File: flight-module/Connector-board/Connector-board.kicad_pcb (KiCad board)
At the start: 4 copper layers, 0 parts

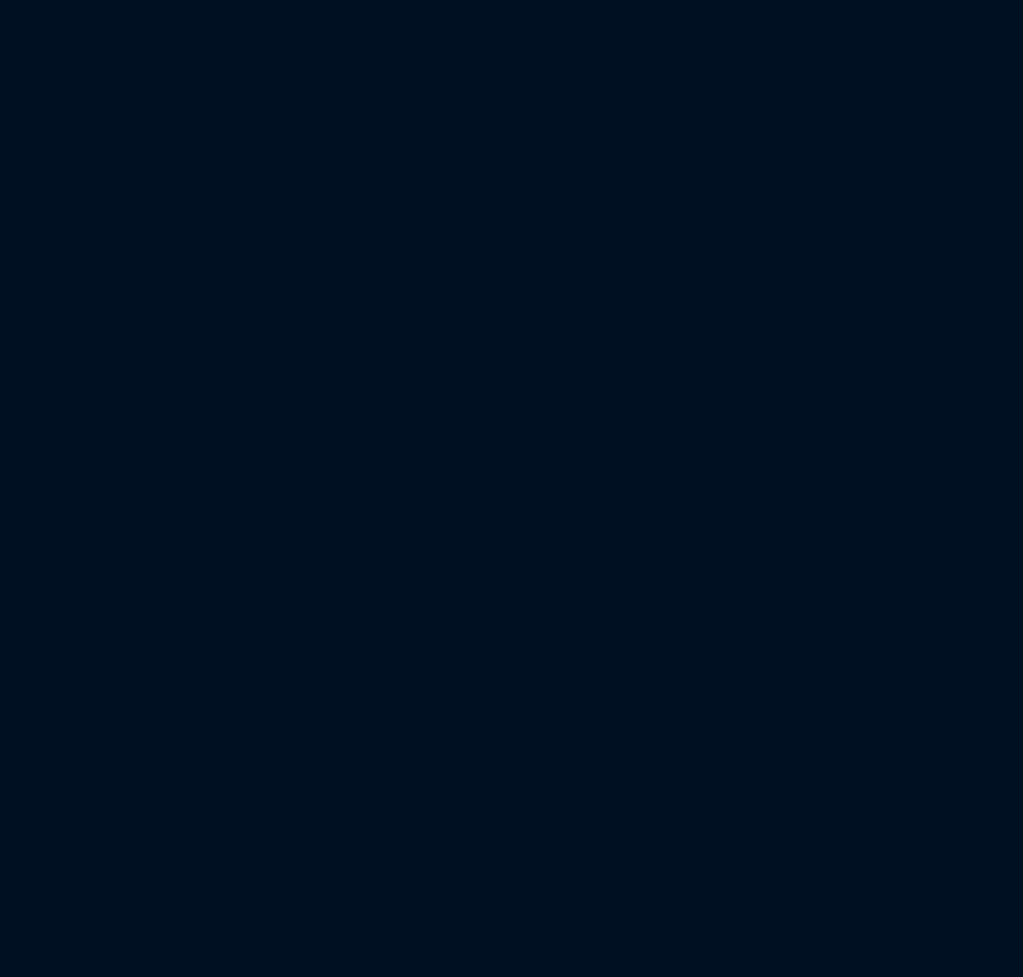
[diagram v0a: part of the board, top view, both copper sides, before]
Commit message: Edited the connector board to make sense
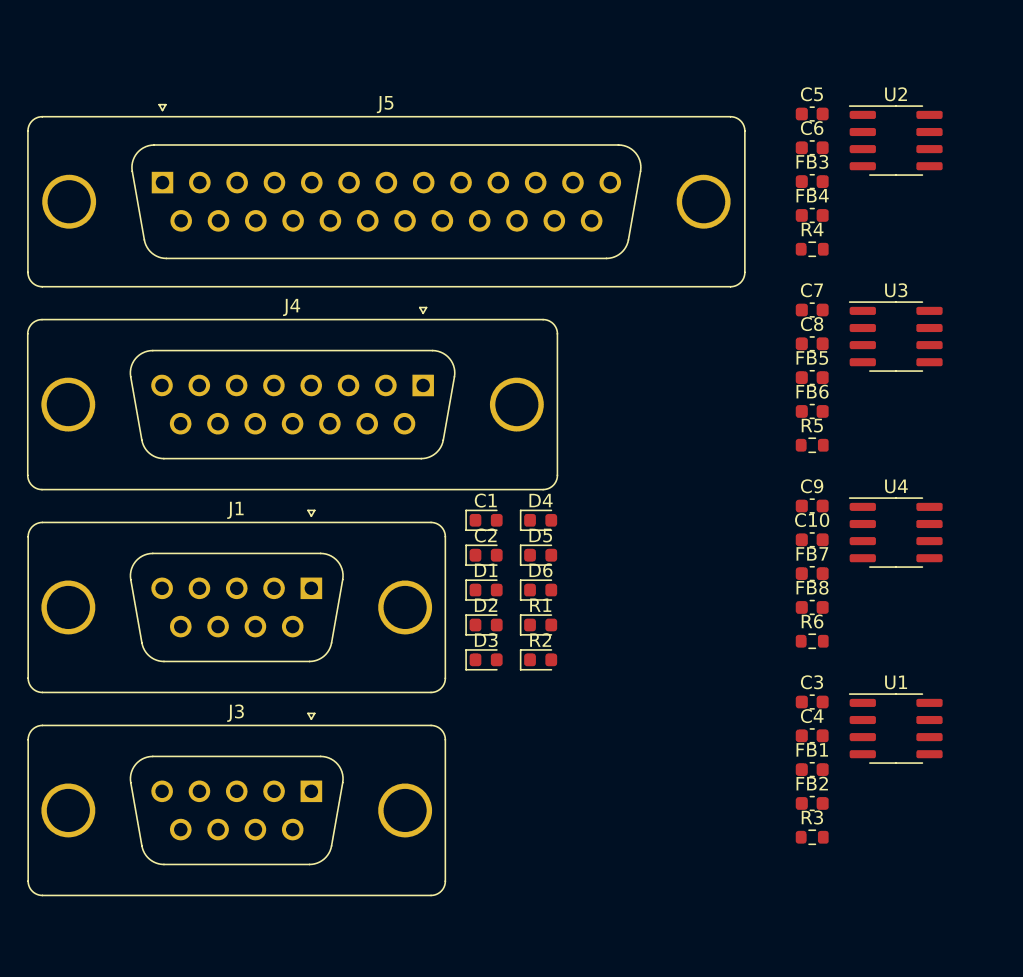
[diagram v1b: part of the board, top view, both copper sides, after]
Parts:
- added C1: 22 µF, Diode_SMD:D_0603_1608Metric, F.Cu at (165.2, 99.5)
- added C10: 10u, Capacitor_SMD:C_0603_1608Metric, F.Cu at (189.4, 100.9)
- added C2: 22 µF, Diode_SMD:D_0603_1608Metric, F.Cu at (165.2, 102.1)
- added C3: 0.01u, Capacitor_SMD:C_0603_1608Metric, F.Cu at (189.4, 113.0)
- added C4: 10u, Capacitor_SMD:C_0603_1608Metric, F.Cu at (189.4, 115.5)
- added C5: 0.01u, Capacitor_SMD:C_0603_1608Metric, F.Cu at (189.4, 69.3)
- added C6: 10u, Capacitor_SMD:C_0603_1608Metric, F.Cu at (189.4, 71.8)
- added C7: 0.01u, Capacitor_SMD:C_0603_1608Metric, F.Cu at (189.4, 83.9)
- added C8: 10u, Capacitor_SMD:C_0603_1608Metric, F.Cu at (189.4, 86.4)
- added C9: 0.01u, Capacitor_SMD:C_0603_1608Metric, F.Cu at (189.4, 98.4)
- added D1: D_Schottky, Diode_SMD:D_0603_1608Metric, F.Cu at (165.2, 104.7)
- added D2: D_Schottky, Diode_SMD:D_0603_1608Metric, F.Cu at (165.2, 107.2)
- added D3: D_Schottky, Diode_SMD:D_0603_1608Metric, F.Cu at (165.2, 109.8)
- added D4: D_Schottky, Diode_SMD:D_0603_1608Metric, F.Cu at (169.3, 99.5)
- added D5: D_Schottky, Diode_SMD:D_0603_1608Metric, F.Cu at (169.3, 102.1)
- added D6: D_Schottky, Diode_SMD:D_0603_1608Metric, F.Cu at (169.3, 104.7)
- added FB1: FerriteBead_Small, Capacitor_SMD:C_0603_1608Metric, F.Cu at (189.4, 118.0)
- added FB2: FerriteBead_Small, Capacitor_SMD:C_0603_1608Metric, F.Cu at (189.4, 120.5)
- added FB3: FerriteBead_Small, Capacitor_SMD:C_0603_1608Metric, F.Cu at (189.4, 74.3)
- added FB4: FerriteBead_Small, Capacitor_SMD:C_0603_1608Metric, F.Cu at (189.4, 76.8)
- added FB5: FerriteBead_Small, Capacitor_SMD:C_0603_1608Metric, F.Cu at (189.4, 88.9)
- added FB6: FerriteBead_Small, Capacitor_SMD:C_0603_1608Metric, F.Cu at (189.4, 91.4)
- added FB7: FerriteBead_Small, Capacitor_SMD:C_0603_1608Metric, F.Cu at (189.4, 103.4)
- added FB8: FerriteBead_Small, Capacitor_SMD:C_0603_1608Metric, F.Cu at (189.4, 105.9)
- added J1: DB9_Female, Connector_Dsub:DSUB-9_Female_Vertical_P2.77x2.84mm_MountingHoles, F.Cu at (152.2, 104.5)
- added J3: DB9_Female, Connector_Dsub:DSUB-9_Female_Vertical_P2.77x2.84mm_MountingHoles, F.Cu at (152.2, 119.6)
- added J4: DB15_Female, Connector_Dsub:DSUB-15_Female_Vertical_P2.77x2.84mm_MountingHoles, F.Cu at (160.5, 89.5)
- added J5: DB25_Receptacle, Connector_Dsub:DSUB-25_Male_Vertical_P2.77x2.84mm_MountingHoles, F.Cu at (141.2, 74.4)
- added R1: 1k, Diode_SMD:D_0603_1608Metric, F.Cu at (169.3, 107.2)
- added R2: 1k, Diode_SMD:D_0603_1608Metric, F.Cu at (169.3, 109.8)
- added R3: 10k, Resistor_SMD:R_0603_1608Metric, F.Cu at (189.4, 123.0)
- added R4: 10k, Resistor_SMD:R_0603_1608Metric, F.Cu at (189.4, 79.4)
- added R5: 10k, Resistor_SMD:R_0603_1608Metric, F.Cu at (189.4, 93.9)
- added R6: 10k, Resistor_SMD:R_0603_1608Metric, F.Cu at (189.4, 108.5)
- added U1: MAX31855KASA, Package_SO:SOIC-8_3.9x4.9mm_P1.27mm, F.Cu at (195.6, 114.9)
- added U2: MAX31855KASA, Package_SO:SOIC-8_3.9x4.9mm_P1.27mm, F.Cu at (195.6, 71.3)
- added U3: MAX31855KASA, Package_SO:SOIC-8_3.9x4.9mm_P1.27mm, F.Cu at (195.6, 85.8)
- added U4: MAX31855KASA, Package_SO:SOIC-8_3.9x4.9mm_P1.27mm, F.Cu at (195.6, 100.4)
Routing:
- net (no net): track 0.00 -> 5309.5 mm
- net 12V: track 363.1 -> 0.00 mm
- net HX5: track 297.7 -> 0.00 mm
- net 3.3V: track 293.4 -> 0.00 mm
- net HX CLK: track 262.4 -> 0.00 mm
- net HX3: track 262.4 -> 0.00 mm
- net SD, TC MISO: track 262.3 -> 0.00 mm
- net HX7: track 241.6 -> 0.00 mm
- net HX1: track 237.9 -> 0.00 mm
- net HX6: track 236.2 -> 0.00 mm
- net HX8: track 233.8 -> 0.00 mm
- net SD, TC CLK: track 228.3 -> 0.00 mm
- net TC CLK: track 223.3 -> 0.00 mm
- net TC MISO: track 215.4 -> 0.00 mm
- net 5V: track 211.1 -> 0.00 mm
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
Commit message: commit edits to the schematic to reflect new pinouts
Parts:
- added J2: Stack_Shape, Stack_Shape:Stack_Shape, F.Cu at (167.6, 94.0)
- moved J5 44.2 mm to (182.4, 58.4), turned to 180 degrees
- moved J3 28.6 mm to (145.9, 91.7), turned to 180 degrees
- moved U2 20.3 mm to (198.1, 91.4)
- moved C4 19.2 mm to (189.4, 134.7)
- moved R3 19.2 mm to (189.4, 142.2)
- moved FB1 19.2 mm to (189.4, 137.2)
- moved FB2 19.2 mm to (189.4, 139.7)
- moved U3 19.1 mm to (198.1, 104.8)
- moved U4 18.5 mm to (198.1, 118.7)
- moved C1 17.5 mm to (165.2, 117.0)
- moved C7 17.5 mm to (189.4, 101.3)
- moved C8 17.5 mm to (189.4, 103.9)
- moved D4 17.5 mm to (169.2, 117.0)
- moved FB6 17.5 mm to (189.4, 108.9)
- moved R5 17.5 mm to (189.4, 111.4)
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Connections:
- net /ETH_Vent renamed /ETH_VENT
- net /LOX_Vent renamed /LOX_VENT
- D1 pad 2: /Ground_ETH_Vent -> GROUND_ETH_VENT
- D2 pad 2: /REDS_ETH_Vent -> REDS_ETH_VENT
- D3 pad 2: /Flight_ETH_Vent -> FLIGHT_ETH_VENT
- D4 pad 2: /Ground_LOX_Vent -> GROUND_LOX_VENT
- D5 pad 2: /REDS_LOX_Vent -> REDS_LOX_VENT
- D6 pad 2: /Flight_LOX_Vent -> FLIGHT_LOX_VENT
- J4 pad 12: REDS_GND -> GND
- J4 pad 13: REDS_ETH -> REDS_ETH_VENT
- J4 pad 14: REDS_LOX_VENT -> GROUND_LOX_VENT
- J4 pad 6: GROUND_LOX_VENT -> REDS_LOX_VENT
- R1 pad 2: GND2 -> GND
- R2 pad 2: GND2 -> GND
- U1 pad 5: SPI1_SCK -> SPI_SCK
- U1 pad 7: SPI1_MISO -> SPI_MISO
- U2 pad 5: SP4_SCK -> SPI_SCK
- U2 pad 7: SP4_MISO -> SPI_MISO
- U3 pad 5: SP2_SCK -> SPI_SCK
- U3 pad 7: SP2_MISO -> SPI_MISO
- U4 pad 5: SPI3_SCK -> SPI_SCK
- U4 pad 7: SPI3_MISO -> SPI_MISO
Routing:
- net (no net): track 5309.5 -> 0.00 mm
- net GND: track 350.6 -> 0.00 mm
- net unconnected-(J5-P25-Pad25): track 47.6 -> 0.00 mm
- net +3.3V: track 28.6 -> 0.00 mm
- net unconnected-(J5-Pad13): track 7.00 -> 0.00 mm
- net TC1_CS: track 0.00 -> 3.46 mm
- net PT1_E+: track 0.00 -> 2.53 mm
- net PT3_A+: track 0.00 -> 0.56 mm
- added copper zone on In2.Cu, net +3.3V
- added copper zone on In1.Cu, net GND
- removed copper zone on B.Cu, net GND
- removed copper zone on F.Cu, net GND
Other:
- board outline added: 141.7 x 134.1 mm

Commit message: completed routing
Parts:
- removed J2: Stack_Shape, Stack_Shape:Stack_Shape
- added J1: Stack_Shape, Stack_Shape:Stack_Shape, F.Cu at (172.7, 106.8)
- D1, D2, D3, D4, D5, D6: footprint Diode_SMD:D_0603_1608Metric -> Diode_SMD:D_SOD-128
- moved U1 84.4 mm to (117.9, 106.1), turned to 90 degrees
- moved C4 80.1 mm to (118.1, 98.2), turned to 180 degrees
- moved FB2 76.1 mm to (117.7, 114.3), turned to 90 degrees
- moved R3 75.7 mm to (122.9, 106.1), turned to -90 degrees
- moved C3 73.4 mm to (118.6, 111.2), turned to 180 degrees
- moved FB1 73.1 mm to (120.0, 114.3), turned to 90 degrees
- moved U4 71.2 mm to (128.0, 106.1), turned to 90 degrees
- moved C10 64.6 mm to (128.1, 98.0), turned to 180 degrees
- moved GND_DSUB1 63.4 mm to (204.2, 124.3), turned to 0 degrees
- moved FB8 62.5 mm to (127.5, 114.5), turned to 90 degrees
- moved C9 61.6 mm to (128.0, 111.2), turned to 180 degrees
- moved FB7 60.0 mm to (129.7, 114.6), turned to 90 degrees
- moved U3 60.0 mm to (138.2, 106.1), turned to 90 degrees
- moved R6 59.7 mm to (133.1, 106.1), turned to -90 degrees
- moved FB6 53.2 mm to (136.5, 114.6), turned to 90 degrees
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- renumbered J3 to 4TC_DSUB1, J4 to GND_DSUB1, J5 to PT_DSUB1, J1 to SOLENOIDS_DSUB1
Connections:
- C1 pad 1: /ETH_VENT -> ETH_VENT
- C2 pad 1: /LOX_VENT -> LOX_VENT
- D1 pad 1: /ETH_VENT -> ETH_VENT
- D2 pad 1: /ETH_VENT -> ETH_VENT
- D3 pad 1: /ETH_VENT -> ETH_VENT
- D4 pad 1: /LOX_VENT -> LOX_VENT
- D5 pad 1: /LOX_VENT -> LOX_VENT
- D6 pad 1: /LOX_VENT -> LOX_VENT
- GND_DSUB1 pad 14: GROUND_LOX_VENT -> REDS_LOX_VENT
- GND_DSUB1 pad 6: REDS_LOX_VENT -> GROUND_LOX_VENT
- PT_DSUB1 pad 10: unconnected-(J5-Pad10) -> PT5_E-
- PT_DSUB1 pad 11: unconnected-(J5-Pad11) -> PT6_E+
- PT_DSUB1 pad 12: unconnected-(J5-Pad12) -> PT6_E-
- PT_DSUB1 pad 15: PT2_E- -> unconnected-(PT_DSUB1-P15-Pad15)
- PT_DSUB1 pad 17: PT3_A+ -> unconnected-(PT_DSUB1-P17-Pad17)
- PT_DSUB1 pad 18: PT4_E- -> PT3_A+
- PT_DSUB1 pad 19: PT4_A+ -> unconnected-(PT_DSUB1-P19-Pad19)
- PT_DSUB1 pad 20: PT5_A+ -> PT4_A+
- PT_DSUB1 pad 21: PT6_E+ -> unconnected-(PT_DSUB1-P21-Pad21)
- PT_DSUB1 pad 22: PT6_E- -> PT5_A+
- PT_DSUB1 pad 24: unconnected-(J5-P24-Pad24) -> PT6_A+
- PT_DSUB1 pad 4: PT3_E+ -> PT2_E-
- PT_DSUB1 pad 5: PT3_E- -> PT3_E+
- PT_DSUB1 pad 6: PT4_E+ -> PT3_E-
- PT_DSUB1 pad 7: PT5_E+ -> PT4_E+
- PT_DSUB1 pad 8: PT5_E- -> PT4_E-
- PT_DSUB1 pad 9: PT6_A+ -> PT5_E+
- SOLENOIDS_DSUB1 pad 1: LOX_VENT+ -> LOX_VENT
- SOLENOIDS_DSUB1 pad 2: ETH_VENT+ -> ETH_VENT
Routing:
- net SPI_SCK: track 0.00 -> 110.3 mm
- net ETH_VENT: track 0.00 -> 104.0 mm
- net SPI_MISO: track 0.00 -> 92.2 mm
- net TC1_CS: track 3.46 -> 85.4 mm, vias 0 -> 2
- net TC4_CS: track 0.00 -> 81.2 mm, vias 0 -> 2
- net TC3_CS: track 0.00 -> 79.9 mm, vias 0 -> 1
- net TC2_CS: track 0.00 -> 72.6 mm, vias 0 -> 1
- net LOX_VENT: track 0.00 -> 72.4 mm
- net PT5_E-: track 0.00 -> 58.7 mm
- net PT5_A+: track 0.00 -> 48.6 mm
- net TC3_T+: track 0.00 -> 47.2 mm
- net FLIGHT_ETH_VENT: track 0.00 -> 42.0 mm, vias 0 -> 1
- net PT6_E+: track 0.00 -> 41.4 mm
- net PT5_E+: track 0.00 -> 40.2 mm, vias 0 -> 2
- net GROUND_ETH_VENT: track 0.00 -> 36.5 mm, vias 0 -> 2
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- added copper zone on F.Cu, net +3.3V
- added copper zone on B.Cu, net +5V
- added copper zone on In2.Cu, net PWR_SUP
- removed copper zone on In2.Cu, net +3.3V
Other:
- board size 141.7 x 134.1 mm -> 134.1 x 141.7 mm

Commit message: Commit - corrections from Dulanya
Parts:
- added D7: D_Schottky, Diode_SMD:D_SOD-128, F.Cu at (176.6, 111.4)
- added D8: D_Schottky, Diode_SMD:D_SOD-128, F.Cu at (176.6, 115.5)
- added G***: LOGO, star:star_8x7, F.Cu at (212.0, 88.1)
- 4TC_DSUB1, GND_DSUB1, PT_DSUB1, SOLENOIDS_DSUB1: moved to B.Cu
- moved PT_DSUB1 6.94 mm to (157.5, 81.1)
- moved 4TC_DSUB1 6.41 mm to (137.6, 133.6)
- moved SOLENOIDS_DSUB1 5.50 mm to (171.7, 98.0)
- moved GND_DSUB1 3.59 mm to (205.5, 127.6)
- moved C6 1.58 mm to (146.7, 98.0)
- moved J1 0.05 mm to (172.6, 106.8)
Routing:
- net GND: track 14.1 -> 58.5 mm, vias 10 -> 17
- net ETH_VENT: track 104.0 -> 125.3 mm
- net GROUND_ETH_VENT: track 36.5 -> 17.7 mm, vias 2 -> 0
- net +3.3V: track 0.00 -> 15.3 mm
- net PT1_E-: track 18.5 -> 30.1 mm
- net REDS_ETH_VENT: track 18.9 -> 30.2 mm, vias 0 -> 2
- net PT1_E+: track 18.9 -> 29.7 mm
- net PT6_E-: track 24.9 -> 35.2 mm, vias 0 -> 1
- net LOX_VENT: track 72.4 -> 82.6 mm
- net PT5_E+: track 40.2 -> 49.7 mm
- net SPI_MISO: track 92.2 -> 99.7 mm
- net SPI_SCK: track 110.3 -> 117.6 mm
- net PT3_E-: track 20.6 -> 27.9 mm, vias 0 -> 1
- net PT4_E-: track 21.6 -> 28.9 mm, vias 0 -> 1
- net PT4_E+: track 21.9 -> 29.2 mm
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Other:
- board text added: "Designed by Ailsa Sun and Space Technologies and Rocketry at UC Berkeley"
- board text added: "Flight Module Connector Board V1"

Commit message: Commit edits part 2
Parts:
- PT_DSUB1: footprint Connector_Dsub:DSUB-25_Male_Vertical_P2.77x2.84mm_MountingHoles -> Connector_Dsub:DSUB-25_Female_Vertical_P2.77x2.84mm_MountingHoles
- moved G*** 8.04 mm to (208.3, 95.2), turned to 90 degrees
- moved PT_DSUB1 2.98 mm to (156.2, 78.5), turned to 180 degrees
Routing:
- net PT1_E-: track 30.1 -> 23.8 mm
- net PT5_E-: track 61.7 -> 67.6 mm
- net PT1_E+: track 29.7 -> 24.7 mm
- net PT6_E-: track 35.2 -> 30.4 mm, vias 1 -> 0
- net PT1_A+: track 24.4 -> 29.1 mm
- net PT4_A+: track 27.5 -> 31.3 mm
- net PT3_A+: track 26.5 -> 30.4 mm
- net PT2_A+: track 25.4 -> 29.2 mm
- net PT6_A+: track 25.8 -> 29.4 mm
- net PT5_A+: track 52.4 -> 55.3 mm
- net PT6_E+: track 41.0 -> 38.8 mm
- net GND: track 58.5 -> 60.7 mm
- net PT4_E+: track 29.2 -> 27.1 mm
- net PT4_E-: track 28.9 -> 26.8 mm
- net PT3_E+: track 28.2 -> 26.1 mm
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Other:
- board text added: "TC 1"
- board text added: "TC 2"
- board text added: "TC 3"
- board text added: "TC 4"
- board text added: "WRONG SIDE"

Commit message: commit - pretty much final unless any major concerns are discovered.
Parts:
- D7, D8: value D_Schottky -> Flyback_Diode; footprint Diode_SMD:D_SOD-128 -> Diode_SMD:CUHS20S40H3F
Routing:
- net SPI_SCK: track 116.2 -> 112.8 mm
- net SPI_MISO: track 99.7 -> 97.1 mm
- net GND: track 60.7 -> 63.2 mm
- net LOX_VENT: track 82.6 -> 83.9 mm
- net TC4_T+: track 22.8 -> 23.4 mm
- net TC1_T-: track 39.3 -> 39.9 mm
- net TC3_T+: track 42.2 -> 42.8 mm
- net TC3_CS: track 83.2 -> 83.8 mm
- net ETH_VENT: track 125.3 -> 124.7 mm
